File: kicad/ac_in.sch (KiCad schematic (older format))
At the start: 42 parts, among them J701 tBlock, J702 tBlock, J703 tBlock, U701 R-78E5.0-1.0, U702 R-78E3.3-1.0, U703 R-78E5.0-1.0, U704 R-78E5.0-1.0, U705 AP2114H-1.2TRG1, U706 AP2114H-1.2TRG1

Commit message: added some 3d models, elminating 15vc and 2 lems
I've elminated 15vc 'cause I don't use these voltage, so I'd change 20w
15v heating power to 10w 5v more efficiency voltage to drive 3.3 and
1.2v to the core and logic. I've also elminated 2 LEMS 'cause space..
even thought there remain 3 for each motor.. more than necesary...keep
going
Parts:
- removed C701: 220uF, servo:C_0603_1608Metric, symbol servo:Capacitor
- removed C705: 22uF, servo:C_0603_1608Metric, symbol servo:Capacitor
- removed C709: 100nF, servo:C_0603_1608Metric, symbol servo:Capacitor
- removed D703: red, servo:LED_0603_1608Metric, symbol servo:LED_A2_K1
- removed J701: tBlock, TerminalBlock_RND:TerminalBlock_RND_205-00288_1x03_P5.08mm_Horizontal, symbol servo:Screw_Terminal_01x03
- removed J702, J703: tBlock, TerminalBlock_RND:TerminalBlock_RND_205-00287_1x02_P5.08mm_Horizontal, symbol servo:Screw_Terminal_01x02
- removed JP703: Jumper_2_Bridged, Jumper:SolderJumper-2_P1.3mm_Open_RoundedPad1.0x1.5mm, symbol servo:Jumper_2_Bridged
- removed PS701, PS702: IRM-15-12, servo:Converter_ACDC_MeanWell_IRM-20-xx_THT, symbol servo:IRM-15-12
- removed R703: 680, Resistor_SMD:R_0603_1608Metric, symbol servo:Resistor
- removed U701, U703: R-78E5.0-1.0, Converter_DCDC:Converter_DCDC_RECOM_R-78E-0.5_THT, symbol servo:R-78E5.0-1.0
- added J701: tblock, servo:tblock02x04, symbol Connector_Generic:Conn_02x04_Row_Letter_Last
- added PS701: IRM-10-5, servo:Converter_ACDC_MeanWell_IRM-10-xx_THT, symbol servo:IRM-10-5
- added PS702: irm-10-12, servo:Converter_ACDC_MeanWell_IRM-10-xx_THT, symbol servo:irm-10-12
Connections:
- net labels added: VBUS_A_N_H, VBUS_A_P_H, VBUS_B_N_H, VBUS_B_P_H
- net labels removed: 15VC
- wire segments 152 -> 130
- no-connect marks 1 -> 0
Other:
- note removed: "5v will have some switching \nnoise, but don't care, couse I'll use \n3v3 for the noise sensible logic.\nIf need some 5v clean supply just add\n a filter near your stuff"
- moved on the sheet: C703, C704, C706, C707, C711, C712, C713, C714, D705, D706, R705, R706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

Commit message: I've reducede the PCB size ADC TVS, USB host and IDC out
TVS for ADC protection, USB out 'cause it's almost free and IDC debug
out in an IDC. Better and thinner terminal block connector help in
reduce the board size.
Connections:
- net at F701.2: now also J701.1b (Pin_1b); no longer J701.2b (Pin_2b)
- net at PS701.2 (AC/N): now also J701.3b (Pin_3b), PS702.2 (AC/N); no longer J701.1b (Pin_1b)
- net at F702.2: now also J701.2b (Pin_2b); no longer J701.3b (Pin_3b)
- net Earth: now reaches J701.4b (Pin_4b)
- net Earth: no longer PS702.2 (AC/N)
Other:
- note added: "Individuali selected input, but in case \nyou want, just join input line pins and \nwith 3 pins turn it all"
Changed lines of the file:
@@
 Connection ~ 3800 2650
-Wire Wire Line
-	3800 6000 3350 6000
-Wire Wire Line
-	3800 2650 3800 6000
-Wire Wire Line
-	3350 6100 3900 6100
-Wire Wire Line
-	3900 6100 3900 2450
 Wire Wire Line
 	3900 2450 4150 2450
@@
 $EndComp
 Wire Wire Line
-	3800 6300 3800 9550
-Wire Wire Line
 	3800 9550 4000 9550
-Wire Wire Line
-	3900 9350 3900 6200
-Wire Wire Line
-	3900 6200 3350 6200
 Wire Wire Line
 	3900 9350 4200 9350
 Connection ~ 4000 9550
-Wire Wire Line
-	3350 6300 3800 6300
 $Comp
 L Connector_Generic:Conn_02x04_Row_Letter_Last J?
@@
 	1    0    0    -1
 $EndComp
+$Comp
+L servo:Earth #PWR?
+U 1 1 5E23C47B
+P 3500 6350
+AR Path="/5DC3DC9E/5E23C47B" Ref="#PWR?"  Part="1"
+AR Path="/5DD76B18/5E23C47B" Ref="#PWR0131"  Part="1"
+F 0 "#PWR0131" H 3500 6100 20  0001 C CNN
+F 1 "Earth" H 3500 6201 20  0000 C CNN
+F 2 "" H 3500 6350 50  0001 C CNN
+F 3 "~" H 3500 6350 50  0001 C CNN
+	1    3500 6350
+	1    0    0    -1
+$EndComp
+Wire Wire Line
+	3350 6300 3500 6300
+Wire Wire Line
+	3500 6300 3500 6350
+Wire Wire Line
+	3350 6200 3800 6200
+Wire Wire Line
+	3800 2650 3800 6200
+Connection ~ 3800 6200
+Wire Wire Line
+	3800 6200 3800 9550
+Wire Wire Line
+	3350 6100 3900 6100
+Wire Wire Line
+	3900 6100 3900 9350
+Wire Wire Line
+	3350 6000 3900 6000
+Wire Wire Line
+	3900 6000 3900 2450
+Text Notes 2800 6500 0    20   ~ 0
+Individuali selected input, but in case \nyou want, just join input line pins and \nwith 3 pins turn it all
 $EndSCHEMATC

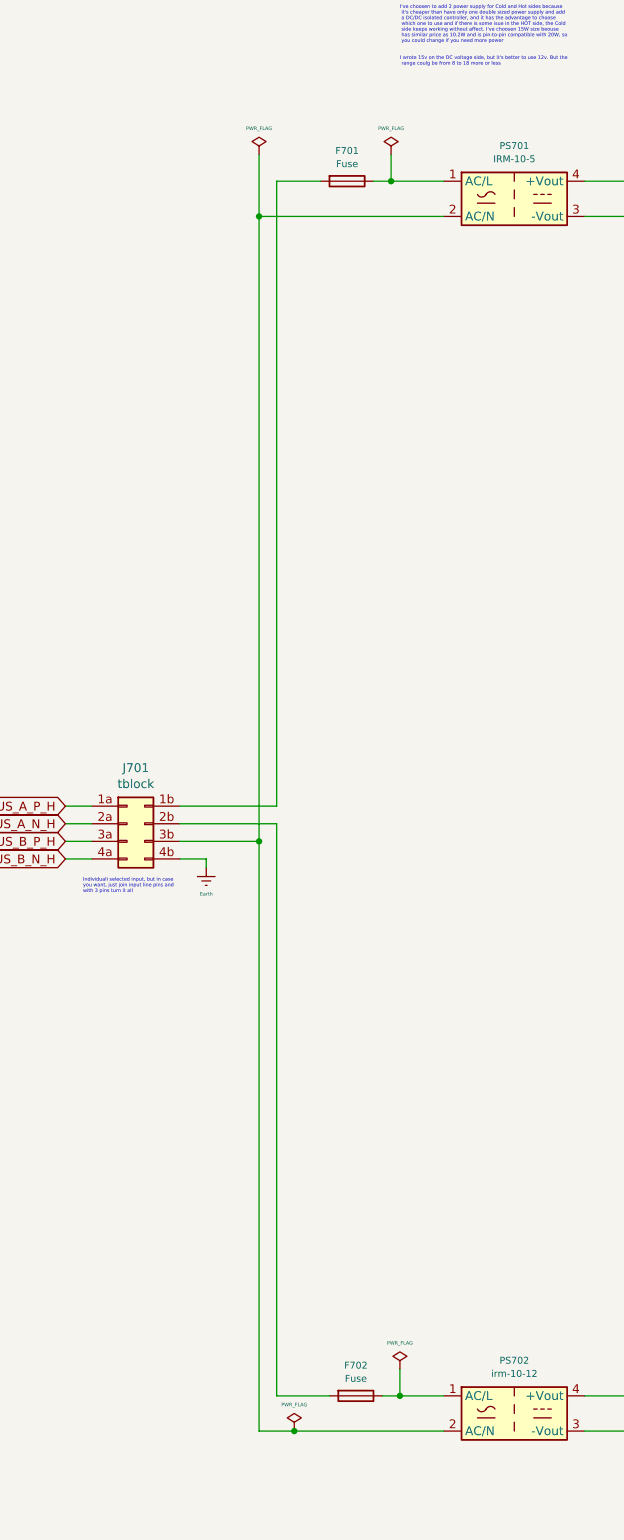
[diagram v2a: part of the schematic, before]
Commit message: I forgot that QUEP was diferential!! all to back....
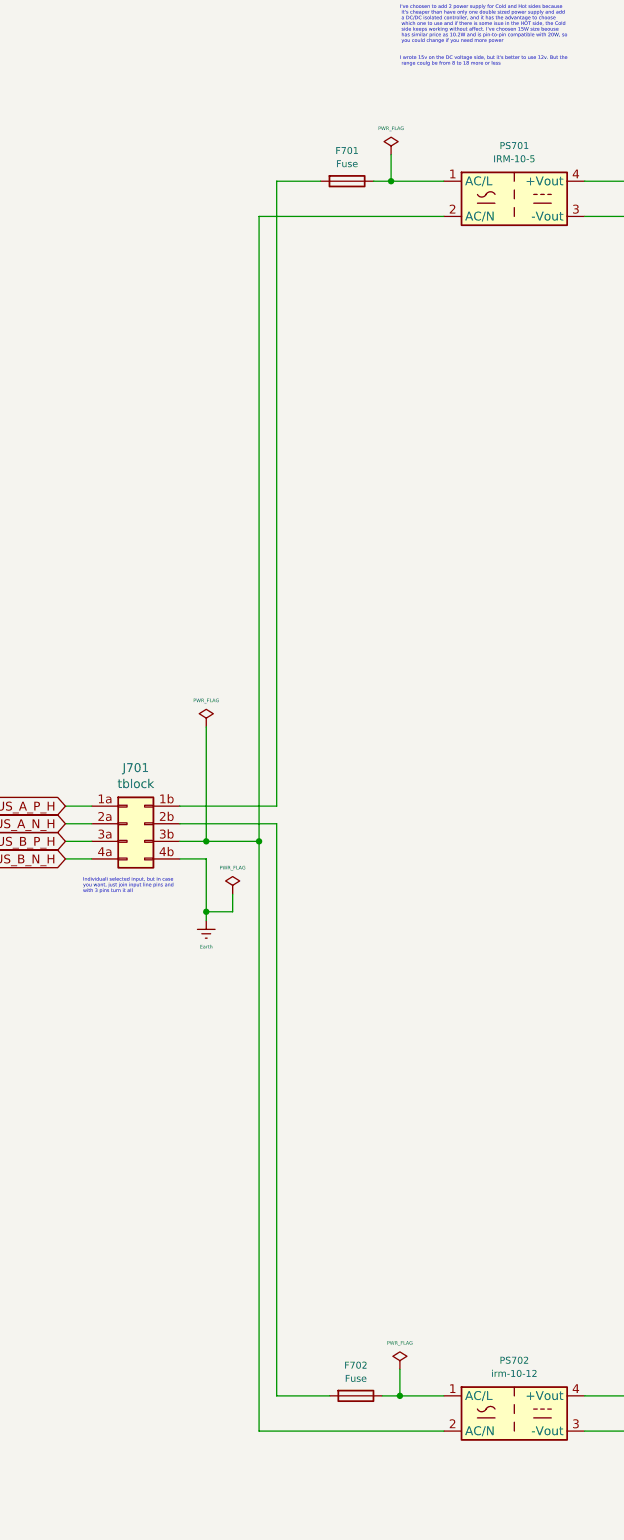
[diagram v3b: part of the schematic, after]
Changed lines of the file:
@@
 $Descr A3 16535 11693
 encoding utf-8
-Sheet 7 18
+Sheet 7 19
 Title "AC input"
 Date "2020-01-09"
@@
 L servo:PWR_FLAG #FLG0701
 U 1 1 5E1BE0A4
-P 3800 2300
-F 0 "#FLG0701" H 3800 2375 20  0001 C CNN
-F 1 "PWR_FLAG" H 3800 2450 20  0000 C CNN
-F 2 "" H 3800 2300 50  0001 C CNN
-F 3 "~" H 3800 2300 50  0001 C CNN
-	1    3800 2300
+P 3500 5550
+F 0 "#FLG0701" H 3500 5625 20  0001 C CNN
+F 1 "PWR_FLAG" H 3500 5700 20  0000 C CNN
+F 2 "" H 3500 5550 50  0001 C CNN
+F 3 "~" H 3500 5550 50  0001 C CNN
+	1    3500 5550
 	1    0    0    -1
 $EndComp
@@
 Wire Wire Line
 	6100 2150 6250 2150
-Wire Wire Line
-	3800 2300 3800 2650
 Connection ~ 4600 9350
 Wire Wire Line
@@
 Wire Wire Line
 	6500 2150 6600 2150
-Connection ~ 3800 2650
 Wire Wire Line
 	3900 2450 4150 2450
-$Comp
-L servo:PWR_FLAG #FLG0706
-U 1 1 5E560C61
-P 4000 9550
-F 0 "#FLG0706" H 4000 9625 20  0001 C CNN
-F 1 "PWR_FLAG" H 4000 9700 20  0000 C CNN
-F 2 "" H 4000 9550 50  0001 C CNN
-F 3 "~" H 4000 9550 50  0001 C CNN
-	1    4000 9550
-	1    0    0    -1
-$EndComp
-Wire Wire Line
-	3800 9550 4000 9550
 Wire Wire Line
 	3900 9350 4200 9350
-Connection ~ 4000 9550
 $Comp
 L Connector_Generic:Conn_02x04_Row_Letter_Last J?
@@
 $EndComp
 Wire Wire Line
-	4000 9550 4850 9550
-Wire Wire Line
 	4600 9350 4850 9350
 Wire Wire Line
@@
 L servo:Earth #PWR?
 U 1 1 5E23C47B
-P 3500 6350
+P 3500 6650
 AR Path="/5DC3DC9E/5E23C47B" Ref="#PWR?"  Part="1"
 AR Path="/5DD76B18/5E23C47B" Ref="#PWR0131"  Part="1"
-F 0 "#PWR0131" H 3500 6100 20  0001 C CNN
-F 1 "Earth" H 3500 6201 20  0000 C CNN
-F 2 "" H 3500 6350 50  0001 C CNN
-F 3 "~" H 3500 6350 50  0001 C CNN
-	1    3500 6350
+F 0 "#PWR0131" H 3500 6400 20  0001 C CNN
+F 1 "Earth" H 3500 6501 20  0000 C CNN
+F 2 "" H 3500 6650 50  0001 C CNN
+F 3 "~" H 3500 6650 50  0001 C CNN
+	1    3500 6650
 	1    0    0    -1
 $EndComp
@@
 	3350 6300 3500 6300
 Wire Wire Line
-	3500 6300 3500 6350
-Wire Wire Line
-	3350 6200 3800 6200
+	3500 6300 3500 6600
+Wire Wire Line
+	3350 6200 3500 6200
 Wire Wire Line
 	3800 2650 3800 6200
@@
 Text Notes 2800 6500 0    20   ~ 0
 Individuali selected input, but in case \nyou want, just join input line pins and \nwith 3 pins turn it all
+$Comp
+L servo:PWR_FLAG #FLG0102
+U 1 1 63A59982
+P 3650 6500
+F 0 "#FLG0102" H 3650 6575 20  0001 C CNN
+F 1 "PWR_FLAG" H 3650 6650 20  0000 C CNN
+F 2 "" H 3650 6500 50  0001 C CNN
+F 3 "~" H 3650 6500 50  0001 C CNN
+	1    3650 6500
+	1    0    0    -1
+$EndComp
+Wire Wire Line
+	3500 6600 3650 6600
+Wire Wire Line
+	3650 6600 3650 6500
+Connection ~ 3500 6600
+Wire Wire Line
+	3500 6600 3500 6650
+Wire Wire Line
+	3800 9550 4850 9550
+Wire Wire Line
+	3500 5550 3500 6200
+Connection ~ 3500 6200
+Wire Wire Line
+	3500 6200 3800 6200
 $EndSCHEMATC

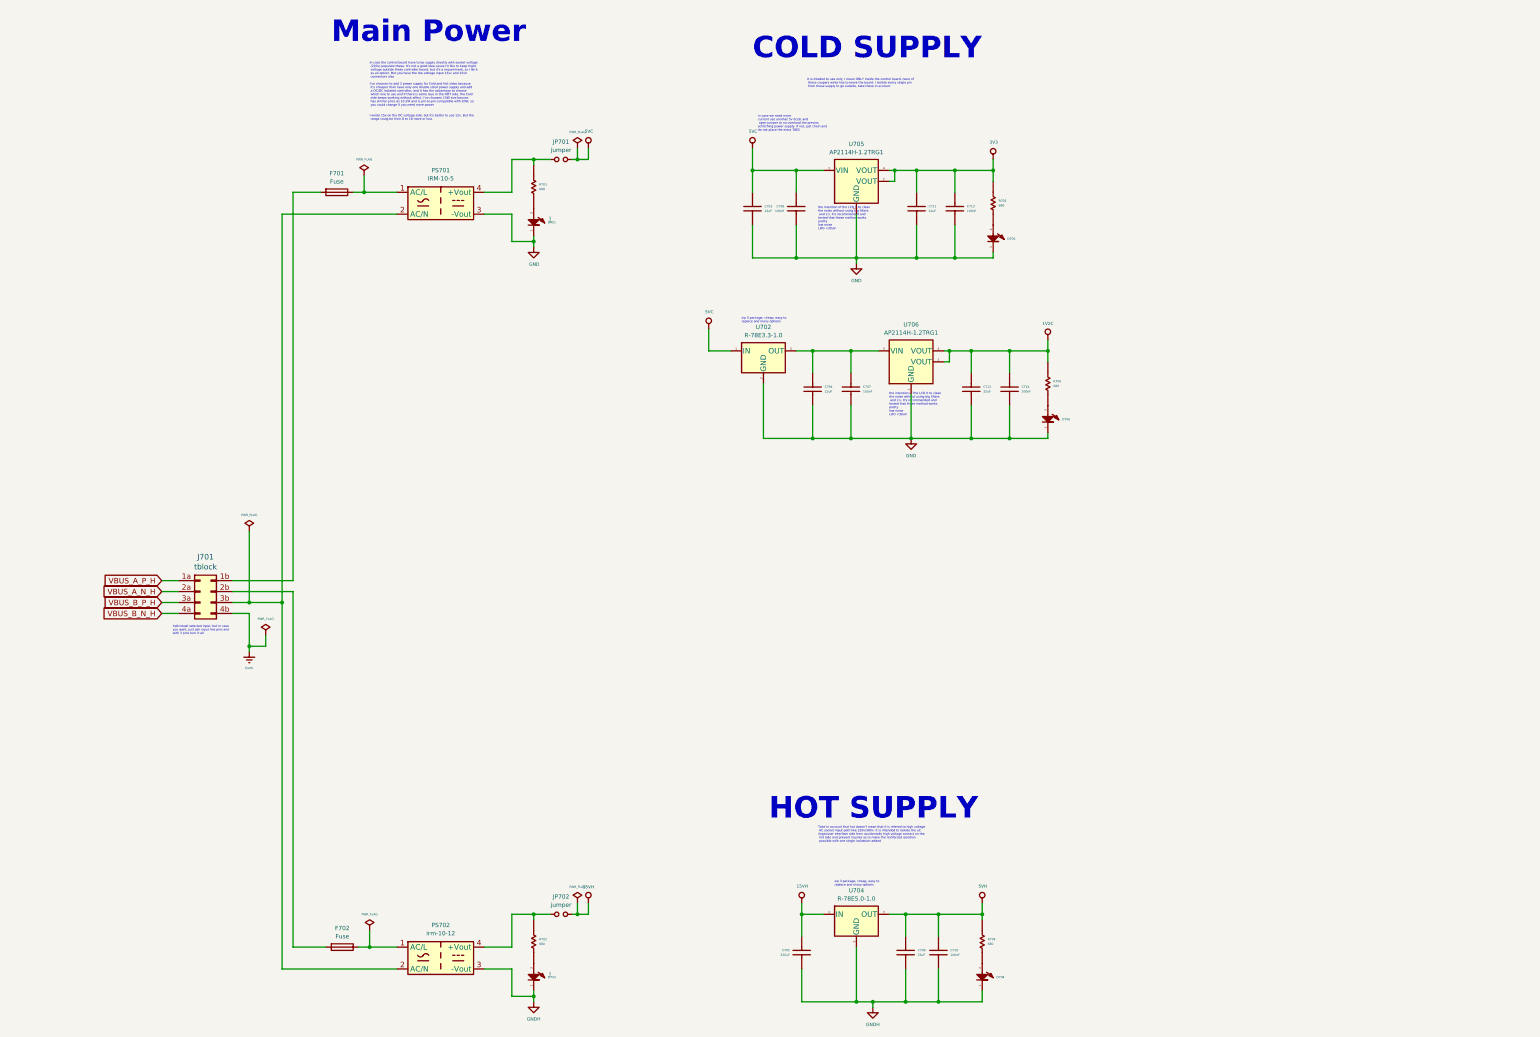
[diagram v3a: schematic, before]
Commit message: changed 200mils connector to 150mils 'cause space constraints
I've decided to change 200 mils input connector for encat, rs485 and so
for 150mis 'cose it doesn't deliver so much current and I'd save some
space in the board. I've added the step/dir differential interface that
I've fotgot, and also add differential input to all signals of
incremental encoder interface A/B/I/S .. now lets rock
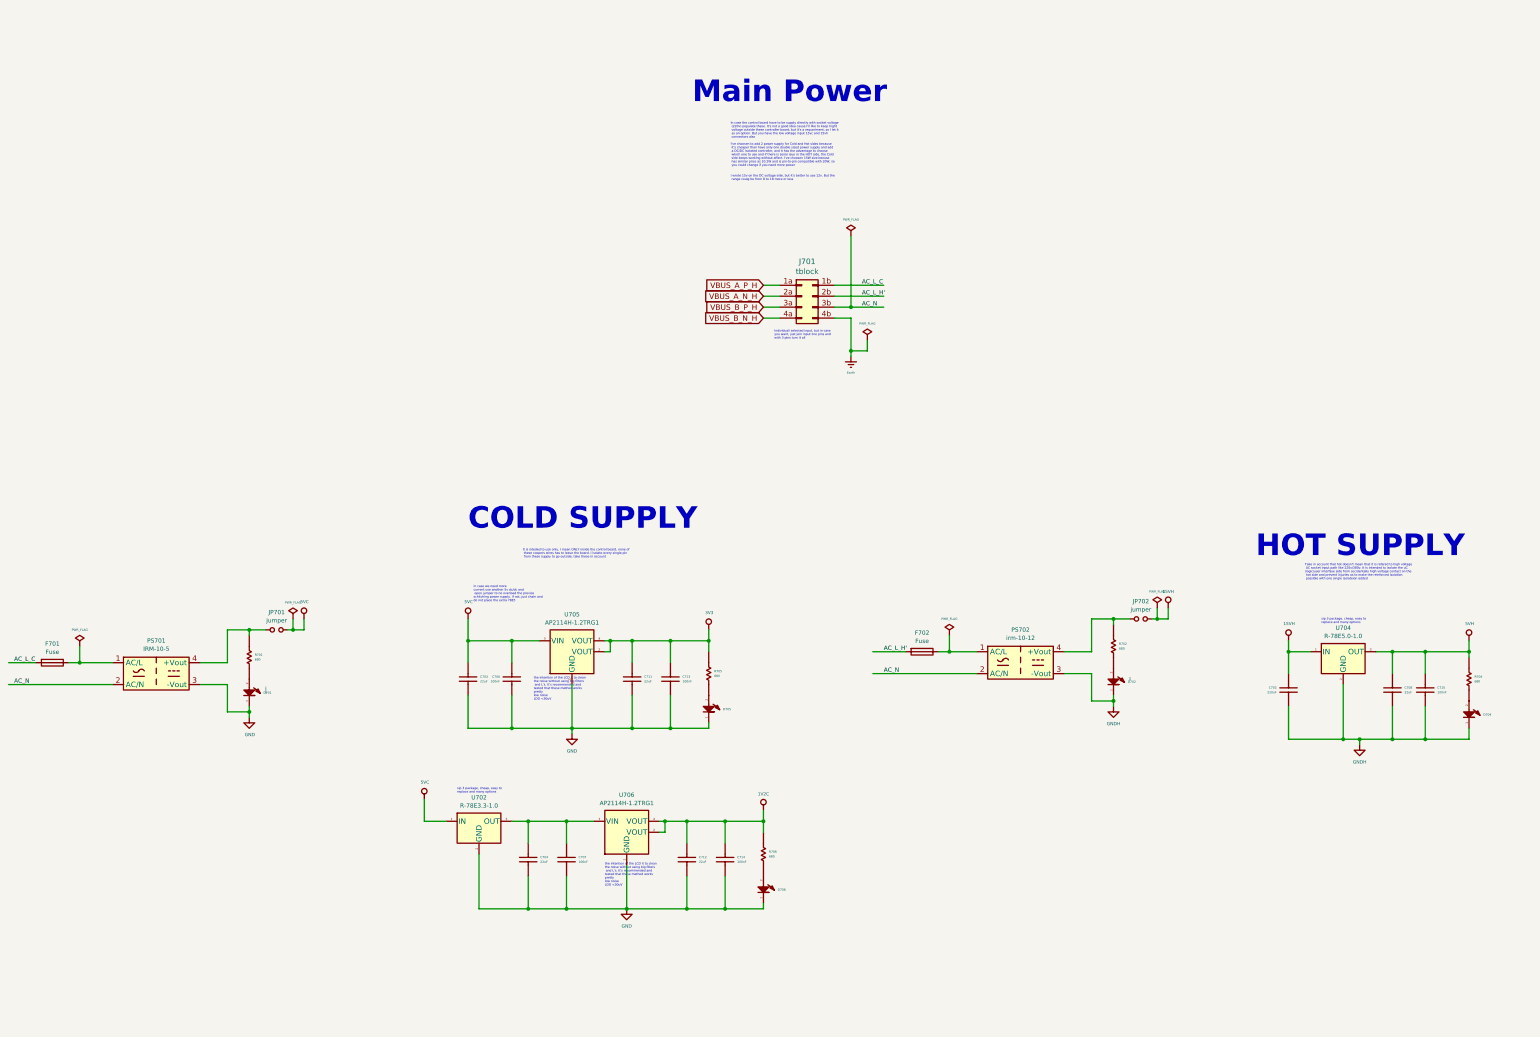
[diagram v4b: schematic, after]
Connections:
- net labels added: AC_L_C, AC_L_H', AC_N
- wire segments 134 -> 130
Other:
- moved on the sheet: C702, C703, C704, C706, C707, C708, C710, C711, C712, C713, C714, D701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

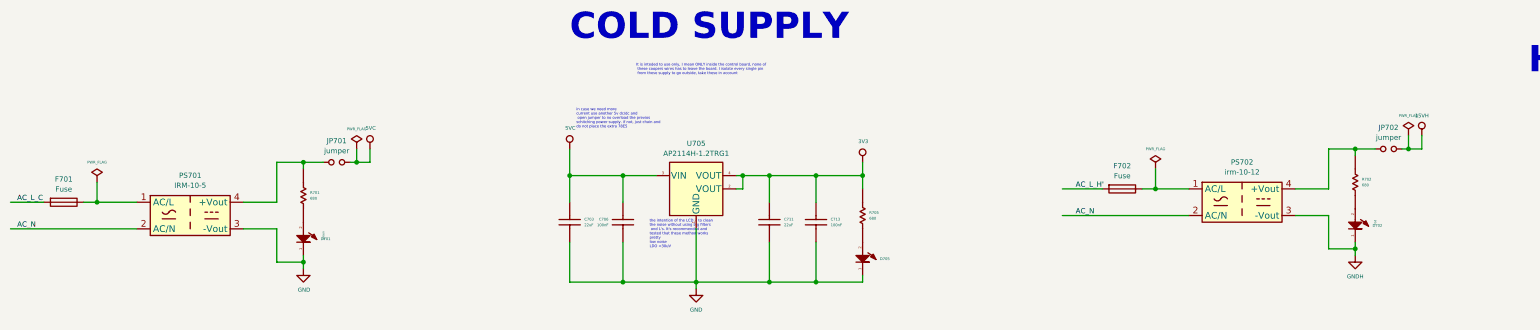
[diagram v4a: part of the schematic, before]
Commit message: All IC placed inside board size but....
I've placed all stuff on board size even thought all are in groups I've
to move the IC to route them. Let's begin
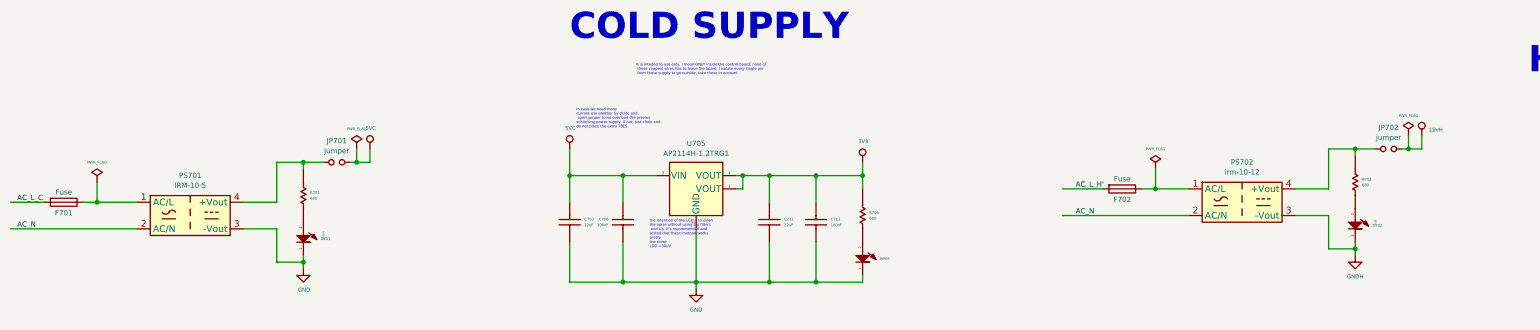
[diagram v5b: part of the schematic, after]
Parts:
- F701, F702: footprint servo:Fuse_1206_3216Metric -> servo:fuse_3912
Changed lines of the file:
@@
 P 11900 6250
 F 0 "#PWR0704" H 11900 6050 20  0001 C CNN
-F 1 "15VH" H 11900 6400 28  0000 C CNN
+F 1 "15VH" H 11953 6294 28  0000 L CNN
 F 2 "" H 11900 6250 50  0001 C CNN
 F 3 "" H 11900 6250 50  0001 C CNN
@@
 U 1 1 5E1D6E68
 P 1700 6750
-F 0 "F701" V 1527 6750 39  0000 C CNN
-F 1 "Fuse" V 1602 6750 39  0000 C CNN
-F 2 "servo:Fuse_1206_3216Metric" V 1630 6750 50  0001 C CNN
-F 3 "~" V 1780 6750 50  0001 C CNN
+F 0 "F701" V 1780 6750 39  0000 C CNN
+F 1 "Fuse" V 1625 6750 39  0000 C CNN
+F 2 "servo:fuse_3912" V 1630 6750 50  0001 C CNN
+F 3 "../doc/datasheets/fuse_3912pdf" V 1780 6750 50  0001 C CNN
 	1    1700 6750
 	0    1    1    0
@@
 U 1 1 5E548509
 P 9650 6650
-F 0 "F702" V 9477 6650 39  0000 C CNN
-F 1 "Fuse" V 9552 6650 39  0000 C CNN
-F 2 "servo:Fuse_1206_3216Metric" V 9580 6650 50  0001 C CNN
-F 3 "~" V 9730 6650 50  0001 C CNN
+F 0 "F702" V 9730 6650 39  0000 C CNN
+F 1 "Fuse" V 9575 6650 39  0000 C CNN
+F 2 "servo:fuse_3912" V 9580 6650 50  0001 C CNN
+F 3 "../doc/datasheets/fuse_3912pdf" V 9730 6650 50  0001 C CNN
 	1    9650 6650
 	0    1    1    0
